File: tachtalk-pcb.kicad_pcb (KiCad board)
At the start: 2 copper layers, 80.2 x 56 mm, 42 parts, among them J1 USB-C breakout module, J2 Screw_Terminal_01x03, SW1 RotaryEncoder_Switch_MP, U1 ESP32-S3-DevKitC, U2 74AHCT1G125, U3 SRV05-4

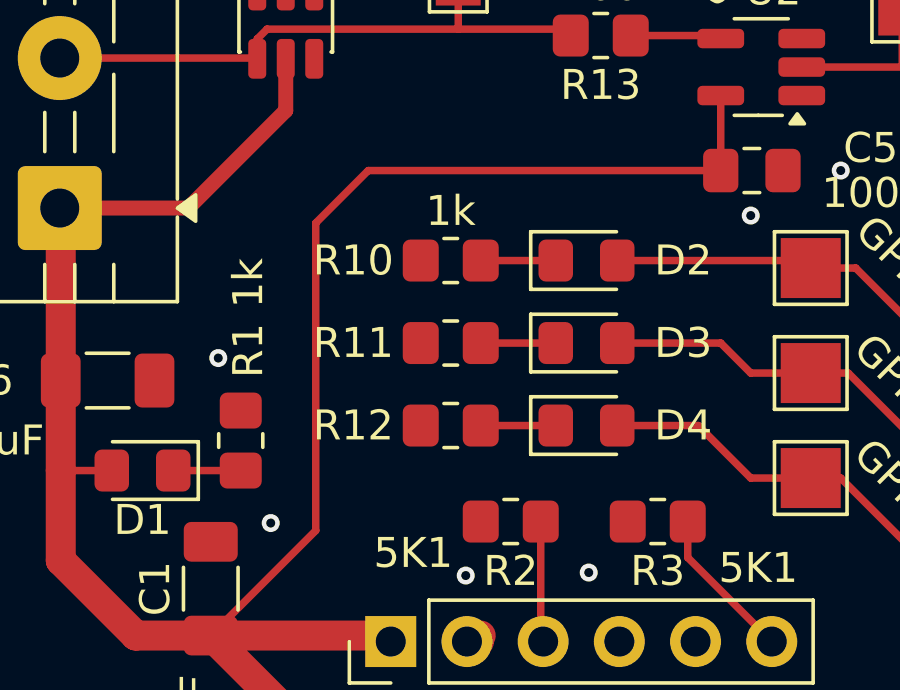
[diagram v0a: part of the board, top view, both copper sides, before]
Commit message: Forgot to update PCB from schematic for Rs
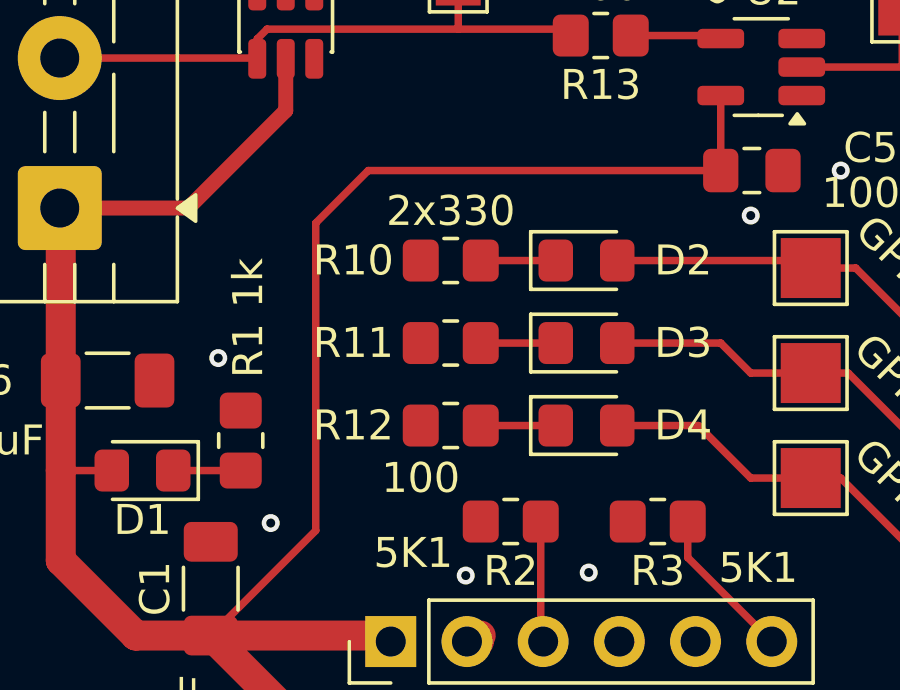
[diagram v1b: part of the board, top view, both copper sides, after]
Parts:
- GPIO10, GPIO11, GPIO4, GPIO5, GPIO6, GPIO7, GPIO9: value ~ -> Testpoint
- R10: value 1k -> 2x330
- R11: value 1k -> 330
- R12: value 1k -> 100
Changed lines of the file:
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@@
 			)
 		)
-		(property "Value" "~"
+		(property "Value" "Testpoint"
 			(at 0 2.05 0)
 			(layer "F.Fab")
@@
 		(sheetname "/")
 		(sheetfile "tachtalk-pcb.kicad_sch")
-		(attr exclude_from_pos_files)
+		(attr exclude_from_pos_files exclude_from_bom)
 		(fp_line
 			(start -1.21 -1.21)
@@
 			)
 		)
-		(property "Value" "~"
+		(property "Value" "Testpoint"
 			(at 0 2.05 0)
 			(layer "F.Fab")
@@
 		(sheetname "/")
 		(sheetfile "tachtalk-pcb.kicad_sch")
-		(attr exclude_from_pos_files)
+		(attr exclude_from_pos_files exclude_from_bom)
 		(fp_line
 			(start -1.21 -1.21)
@@
 			)
 		)
-		(property "Value" "~"
+		(property "Value" "Testpoint"
 			(at 0 2.05 0)
 			(layer "F.Fab")
@@
 		(sheetname "/")
 		(sheetfile "tachtalk-pcb.kicad_sch")
-		(attr exclude_from_pos_files)
+		(attr exclude_from_pos_files exclude_from_bom)
 		(fp_line
 			(start -1.21 -1.21)
@@
 			)
 		)
-		(property "Value" "~"
+		(property "Value" "Testpoint"
 			(at 0 2.05 0)
 			(layer "F.Fab")
@@
 		(sheetname "/")
 		(sheetfile "tachtalk-pcb.kicad_sch")
-		(attr exclude_from_pos_files)
+		(attr exclude_from_pos_files exclude_from_bom)
 		(fp_line
 			(start -1.21 -1.21)
@@
 			)
 		)
-		(property "Value" "1k"
+		(property "Value" "330"
 			(at 0 1.65 0)
 			(layer "F.Fab")
@@
 			)
 		)
-		(property "LCSC Part #" "C17513"
+		(property "LCSC Part #" "C17630"
 			(at 0 0 180)
 			(unlocked yes)
@@
 			)
 		)
-		(property "Value" "~"
+		(property "Value" "Testpoint"
 			(at 0 2.05 0)
 			(layer "F.Fab")
@@
 		(sheetname "/")
 		(sheetfile "tachtalk-pcb.kicad_sch")
-		(attr exclude_from_pos_files)
+		(attr exclude_from_pos_files exclude_from_bom)
 		(fp_line
 			(start -1.21 -1.21)
@@
 			)
 		)
-		(property "Value" "~"
+		(property "Value" "Testpoint"
 			(at 0 2.05 0)
 			(layer "F.Fab")
@@
 		(sheetname "/")
 		(sheetfile "tachtalk-pcb.kicad_sch")
-		(attr exclude_from_pos_files)
+		(attr exclude_from_pos_files exclude_from_bom)
 		(fp_line
 			(start -1.21 -1.21)
@@
 		(sheetname "/")
 		(sheetfile "tachtalk-pcb.kicad_sch")
-		(attr exclude_from_pos_files)
+		(attr exclude_from_pos_files exclude_from_bom)
 		(fp_line
 			(start -0.96 -0.96)
@@
 			)
 		)
-		(property "Value" "1k"
-			(at 0 1.65 0)
-			(layer "F.Fab")
-			(hide yes)
+		(property "Value" "100"
+			(at 1 -1.75 0)
+			(layer "F.SilkS")
 			(effects
 				(font
@@
 			)
 		)
-		(property "LCSC Part #" "C17513"
+		(property "LCSC Part #" "C17408"
 			(at 0 0 180)
 			(unlocked yes)
@@
 			)
 		)
-		(property "Value" "1k"
+		(property "Value" "2x330"
 			(at 0 1.65 0)
 			(layer "F.SilkS")
@@
 			)
 		)
-		(property "LCSC Part #" "C17513"
+		(property "LCSC Part #" "C17630"
 			(at 0 0 180)
 			(unlocked yes)
@@
 			)
 		)
-		(property "Value" "~"
+		(property "Value" "Testpoint"
 			(at 0 2.05 0)
 			(layer "F.Fab")
@@
 		(sheetname "/")
 		(sheetfile "tachtalk-pcb.kicad_sch")
-		(attr exclude_from_pos_files)
+		(attr exclude_from_pos_files exclude_from_bom)
 		(fp_line
 			(start -1.21 -1.21)
@@
 		(sheetname "/")
 		(sheetfile "tachtalk-pcb.kicad_sch")
-		(attr exclude_from_pos_files)
+		(attr exclude_from_pos_files exclude_from_bom)
 		(fp_line
 			(start -0.96 -0.96)
@@
 		)
 		(fp_text user "GND"
+			(at 22.86 0 0)
+			(unlocked yes)
+			(layer "F.SilkS")
+			(effects
+				(font
+					(size 1 1)
+					(thickness 0.15)
+				)
+				(justify right)
+			)
+		)
+		(fp_text user "GND"
 			(at 1.52032 53.33728 0)
 			(unlocked yes)
@@
 			(unlocked yes)
 			(layer "F.SilkS")
-			(effects
-				(font
-					(size 1 1)
-					(thickness 0.15)
-				)
-				(justify right)
-			)
-		)
-		(fp_text user "GND"
-			(at 22.86 0 0)
-			(unlocked yes)
-			(layer "F.SilkS")

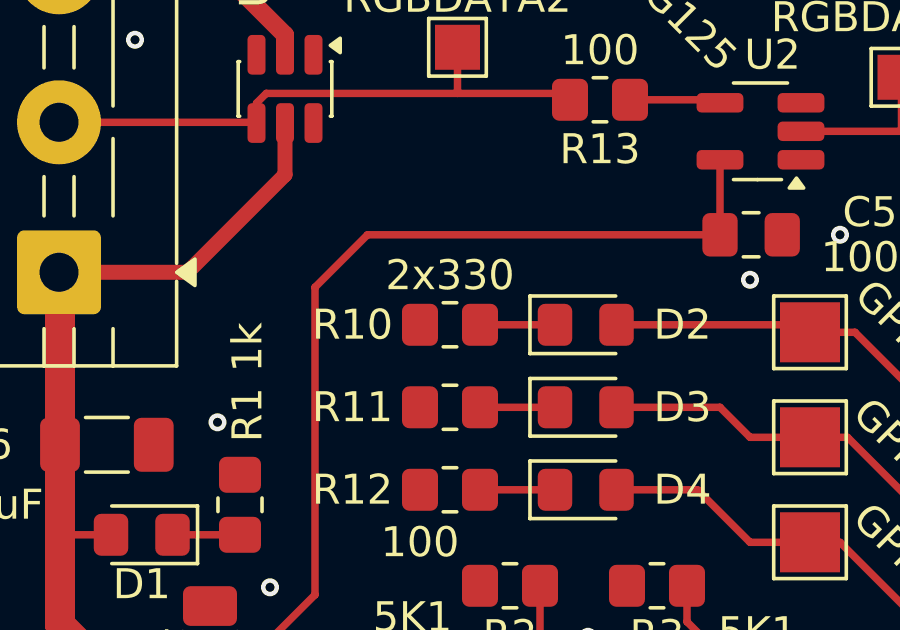
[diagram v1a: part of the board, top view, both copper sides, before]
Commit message: Make R values proper
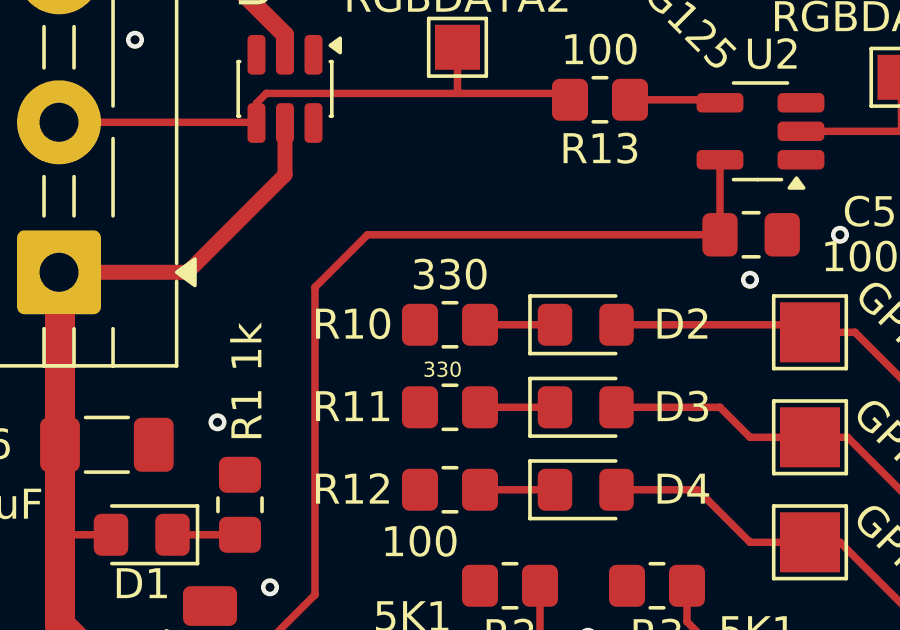
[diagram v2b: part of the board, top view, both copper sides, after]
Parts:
- R10: value 2x330 -> 330
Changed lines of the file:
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@@
 		)
 		(property "Value" "330"
-			(at 0 1.65 0)
-			(layer "F.Fab")
-			(hide yes)
-			(effects
-				(font
-					(size 1 1)
-					(thickness 0.15)
+			(at 0.25 1.25 0)
+			(layer "F.SilkS")
+			(effects
+				(font
+					(size 0.5 0.5)
+					(thickness 0.125)
 				)
 			)
@@
 			)
 		)
-		(property "Value" "2x330"
+		(property "Value" "330"
 			(at 0 1.65 0)
 			(layer "F.SilkS")

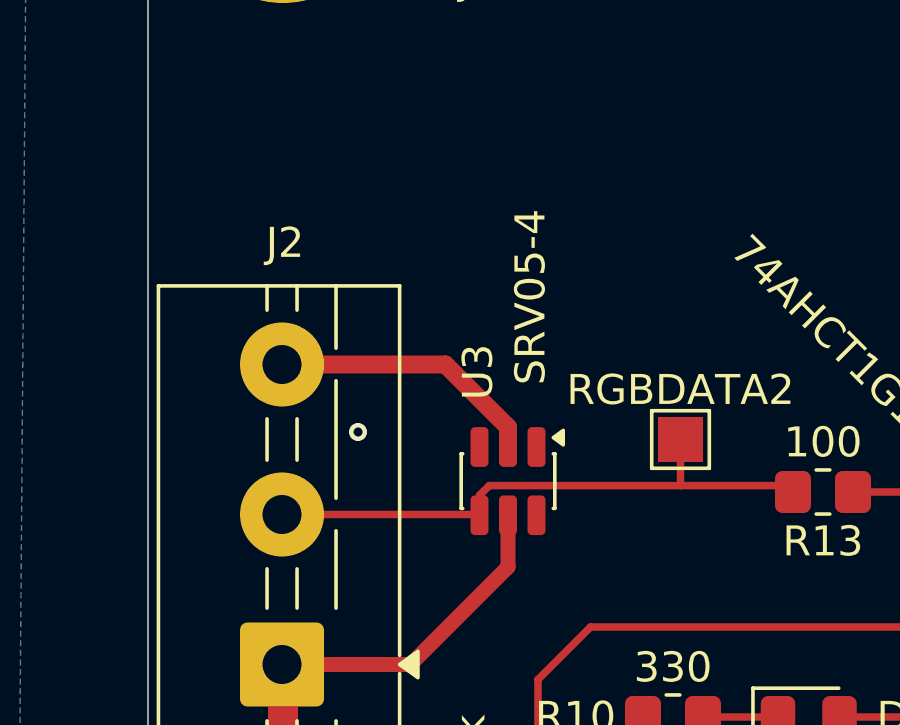
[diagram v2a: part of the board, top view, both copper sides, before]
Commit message: Fix wrong footprint
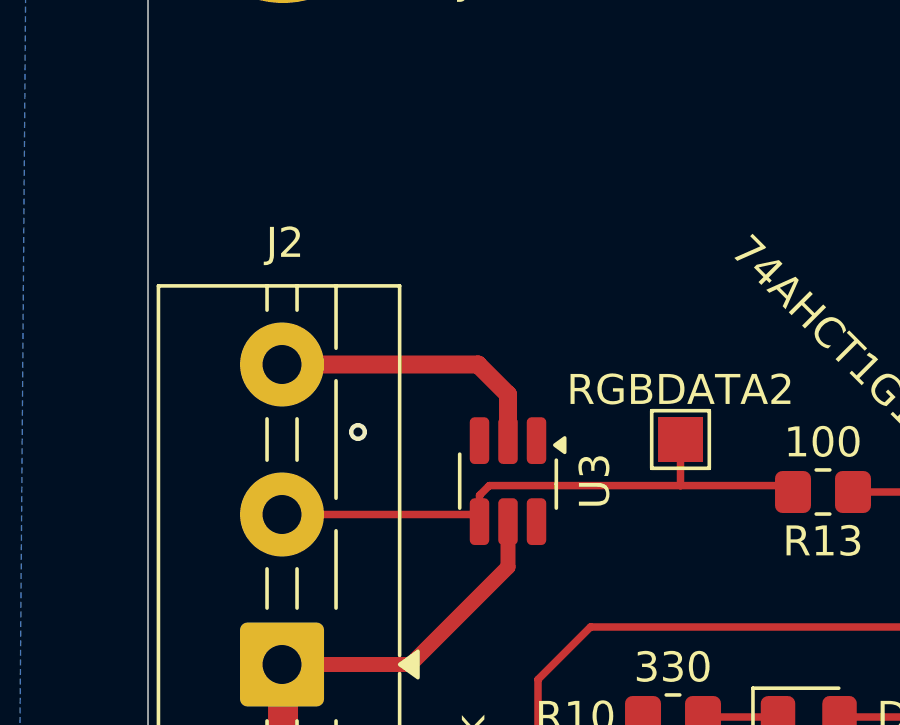
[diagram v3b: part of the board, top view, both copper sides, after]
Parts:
- U3: footprint Package_TO_SOT_SMD:SOT-23-6 -> Package_TO_SOT_SMD:SOT-23-6_Handsoldering
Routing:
- net GND: track 9.34 -> 10.4 mm
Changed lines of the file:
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@@
 		)
 	)
-	(footprint "Package_TO_SOT_SMD:SOT-23-6"
+	(footprint "Package_TO_SOT_SMD:SOT-23-6_Handsoldering"
 		(layer "F.Cu")
 		(at 31.5 96.6375 -90)
-		(descr "SOT, 6 Pin (JEDEC MO-178 Var AB https://www.jedec.org/document_search?search_api_views_fulltext=MO-178), generated with kicad-footprint-generator ipc_gullwing_generator.py")
-		(tags "SOT TO_SOT_SMD")
+		(descr "6-pin SOT-23 package, Handsoldering")
+		(tags "SOT-23-6 Handsoldering")
 		(property "Reference" "U3"
-			(at -3.6375 1 90)
+			(at 0 -2.9 270)
 			(layer "F.SilkS")
 			(effects
@@
 		)
 		(property "Value" "SRV05-4"
-			(at -6.1375 -0.75 90)
-			(layer "F.SilkS")
+			(at 0 2.9 270)
+			(layer "F.Fab")
 			(effects
 				(font
@@
 		)
 		(property "Datasheet" "http://www.onsemi.com/pub/Collateral/SRV05-4-D.PDF"
-			(at 0 0 90)
+			(at 0 0 270)
+			(unlocked yes)
 			(layer "F.Fab")
 			(hide yes)
@@
 		)
 		(property "Description" "ESD Protection Diodes with Low Clamping Voltage, SOT-23-6"
-			(at 0 0 90)
+			(at 0 0 270)
+			(unlocked yes)
 			(layer "F.Fab")
 			(hide yes)
@@
 		(attr smd)
 		(fp_line
-			(start -0.91 1.56)
-			(end -0.91 1.51)
-			(stroke
-				(width 0.12)
-				(type solid)
-			)
-			(layer "F.SilkS")
-		)
-		(fp_line
-			(start 0.91 1.56)
-			(end -0.91 1.56)
-			(stroke
-				(width 0.12)
-				(type solid)
-			)
-			(layer "F.SilkS")
-		)
-		(fp_line
-			(start 0.91 1.51)
-			(end 0.91 1.56)
-			(stroke
-				(width 0.12)
-				(type solid)
-			)
-			(layer "F.SilkS")
-		)
-		(fp_line
-			(start -0.91 -1.51)
-			(end -0.91 -1.56)
+			(start -0.9 1.61)
+			(end 0.9 1.61)
 			(stroke
 				(width 0.12)
@@
 		)
 		(fp_line
-			(start -0.91 -1.56)
-			(end 0.91 -1.56)
+			(start 0.1 -1.61)
+			(end -0.7 -1.61)
 			(stroke
 				(width 0.12)
@@
 		)
 		(fp_line
-			(start 0.91 -1.56)
-			(end 0.91 -1.51)
+			(start 0.1 -1.61)
+			(end 0.9 -1.61)
 			(stroke
 				(width 0.12)
@@
 		(fp_poly
 			(pts
-				(xy -1.45 -1.51) (xy -1.69 -1.84) (xy -1.21 -1.84)
+				(xy -1.2 -1.56) (xy -1.44 -1.89) (xy -0.96 -1.89) (xy -1.2 -1.56)
 			)
 			(stroke
@@
 		)
 		(fp_line
-			(start -1.050001 1.7)
-			(end -1.05 1.5)
-			(stroke
-				(width 0.05)
-				(type solid)
-			)
-			(layer "F.CrtYd")
-		)
-		(fp_line
-			(start 1.050001 1.7)
-			(end -1.050001 1.7)
+			(start -2.4 1.8)
+			(end -2.4 -1.8)
 			(stroke
 				(width 0.05)
@@
 		)
 		(fp_line
-			(start -2.05 1.5)
-			(end -2.05 -1.5)
+			(start 2.4 1.8)
+			(end -2.4 1.8)
 			(stroke
 				(width 0.05)
@@
 		)
 		(fp_line
-			(start -1.05 1.5)
-			(end -2.05 1.5)
+			(start -2.4 -1.8)
+			(end 2.4 -1.8)
 			(stroke
 				(width 0.05)
@@
 		)
 		(fp_line
-			(start 1.05 1.5)
-			(end 1.050001 1.7)
+			(start 2.4 -1.8)
+			(end 2.4 1.8)
 			(stroke
 				(width 0.05)
@@
 		)
 		(fp_line
-			(start 2.05 1.5)
-			(end 1.05 1.5)
+			(start 0.9 1.55)
+			(end -0.9 1.55)
 			(stroke
-				(width 0.05)
-				(type solid)
-			)
-			(layer "F.CrtYd")
-		)
-		(fp_line
-			(start -2.05 -1.5)
-			(end -1.05 -1.5)
-			(stroke
-				(width 0.05)
-				(type solid)
-			)
-			(layer "F.CrtYd")
-		)
-		(fp_line
-			(start -1.05 -1.5)
-			(end -1.050001 -1.7)
-			(stroke
-				(width 0.05)
+				(width 0.1)
 				(type solid)
 			)
-			(layer "F.CrtYd")
+			(layer "F.Fab")
 		)
 		(fp_line
-			(start 1.05 -1.5)
-			(end 2.05 -1.5)
+			(start -0.9 -0.9)
+			(end -0.9 1.55)
 			(stroke
-				(width 0.05)
+				(width 0.1)
 				(type solid)
 			)
-			(layer "F.CrtYd")
+			(layer "F.Fab")
 		)
 		(fp_line
-			(start 2.05 -1.5)
-			(end 2.05 1.5)
+			(start -0.9 -0.9)
+			(end -0.25 -1.55)
 			(stroke
-				(width 0.05)
+				(width 0.1)
 				(type solid)
 			)
-			(layer "F.CrtYd")
+			(layer "F.Fab")
 		)
 		(fp_line
-			(start -1.050001 -1.7)
-			(end 1.050001 -1.7)
+			(start 0.9 -1.55)
+			(end 0.9 1.55)
 			(stroke
-				(width 0.05)
+				(width 0.1)
 				(type solid)
 			)
-			(layer "F.CrtYd")
+			(layer "F.Fab")
 		)
 		(fp_line
-			(start 1.050001 -1.7)
-			(end 1.05 -1.5)
-			(stroke
-				(width 0.05)
-				(type solid)
-			)
-			(layer "F.CrtYd")
-		)
-		(fp_poly
-			(pts
-				(xy -0.4 -1.45) (xy 0.8 -1.45) (xy 0.8 1.45) (xy -0.8 1.45) (xy -0.8 -1.050001)
-			)
+			(start 0.9 -1.55)
+			(end -0.25 -1.55)
 			(stroke
 				(width 0.1)
 				(type solid)
 			)
-			(fill no)
 			(layer "F.Fab")
 		)
@@
 			(effects
 				(font
-					(size 0.72 0.72)
-					(thickness 0.11)
+					(size 0.5 0.5)
+					(thickness 0.075)
 				)
 			)
 		)
 		(pad "1" smd roundrect
-			(at -1.1375 -0.949999 270)
-			(size 1.325 0.6)
+			(at -1.35 -0.95 270)
+			(size 1.56 0.65)
 			(layers "F.Cu" "F.Mask" "F.Paste")
 			(roundrect_rratio 0.25)
@@
 		)
 		(pad "2" smd roundrect
-			(at -1.1375 0 270)
-			(size 1.325 0.6)
+			(at -1.35 0 270)
+			(size 1.56 0.65)
 			(layers "F.Cu" "F.Mask" "F.Paste")
 			(roundrect_rratio 0.25)
@@
 		)
 		(pad "3" smd roundrect
-			(at -1.1375 0.949999 270)
-			(size 1.325 0.6)
+			(at -1.35 0.95 270)
+			(size 1.56 0.65)
 			(layers "F.Cu" "F.Mask" "F.Paste")
 			(roundrect_rratio 0.25)
@@
 		)
 		(pad "4" smd roundrect
-			(at 1.1375 0.949999 270)
-			(size 1.325 0.6)
+			(at 1.35 0.95 270)
+			(size 1.56 0.65)
 			(layers "F.Cu" "F.Mask" "F.Paste")
 			(roundrect_rratio 0.25)
@@
 		)
 		(pad "5" smd roundrect
-			(at 1.1375 0 270)
-			(size 1.325 0.6)
+			(at 1.35 0 270)
+			(size 1.56 0.65)
 			(layers "F.Cu" "F.Mask" "F.Paste")
 			(roundrect_rratio 0.25)
@@
 		)
 		(pad "6" smd roundrect
-			(at 1.1375 -0.949999 270)
-			(size 1.325 0.6)
+			(at 1.35 -0.95 270)
+			(size 1.56 0.65)
 			(layers "F.Cu" "F.Mask" "F.Paste")
 			(roundrect_rratio 0.25)
@@
 	)
 	(segment
-		(start 31.5 95.5)
-		(end 31.5 94.837501)
+		(start 31.5 93.75)
+		(end 31.5 95.2875)
 		(width 0.6)
 		(layer "F.Cu")
@@
 	)
 	(segment
-		(start 31.5 94.837501)
-		(end 29.412499 92.75)
+		(start 30.5 92.75)
+		(end 31.5 93.75)
 		(width 0.6)
 		(layer "F.Cu")
@@
 	)
 	(segment
-		(start 29.412499 92.75)
-		(end 23.9675 92.75)
+		(start 31.5 95.5)
+		(end 31.5 94.837501)
 		(width 0.6)
 		(layer "F.Cu")
@@
 		(layer "F.Cu")
 		(net 15)
+	)
+	(segment
+		(start 23.9675 92.75)
+		(end 30.5 92.75)
+		(width 0.6)
+		(layer "F.Cu")
+		(net 15)
